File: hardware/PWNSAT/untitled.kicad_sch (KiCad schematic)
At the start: 67 parts, among them J2 Conn_01x04_Pin, J4 Conn_01x03, P4 USB_C_Plug_USB2.0, SW2 SW_Push, SW3 SW_Push, U6 W25N02KVZEIR, Y1 Crystal, Y2 24MHz

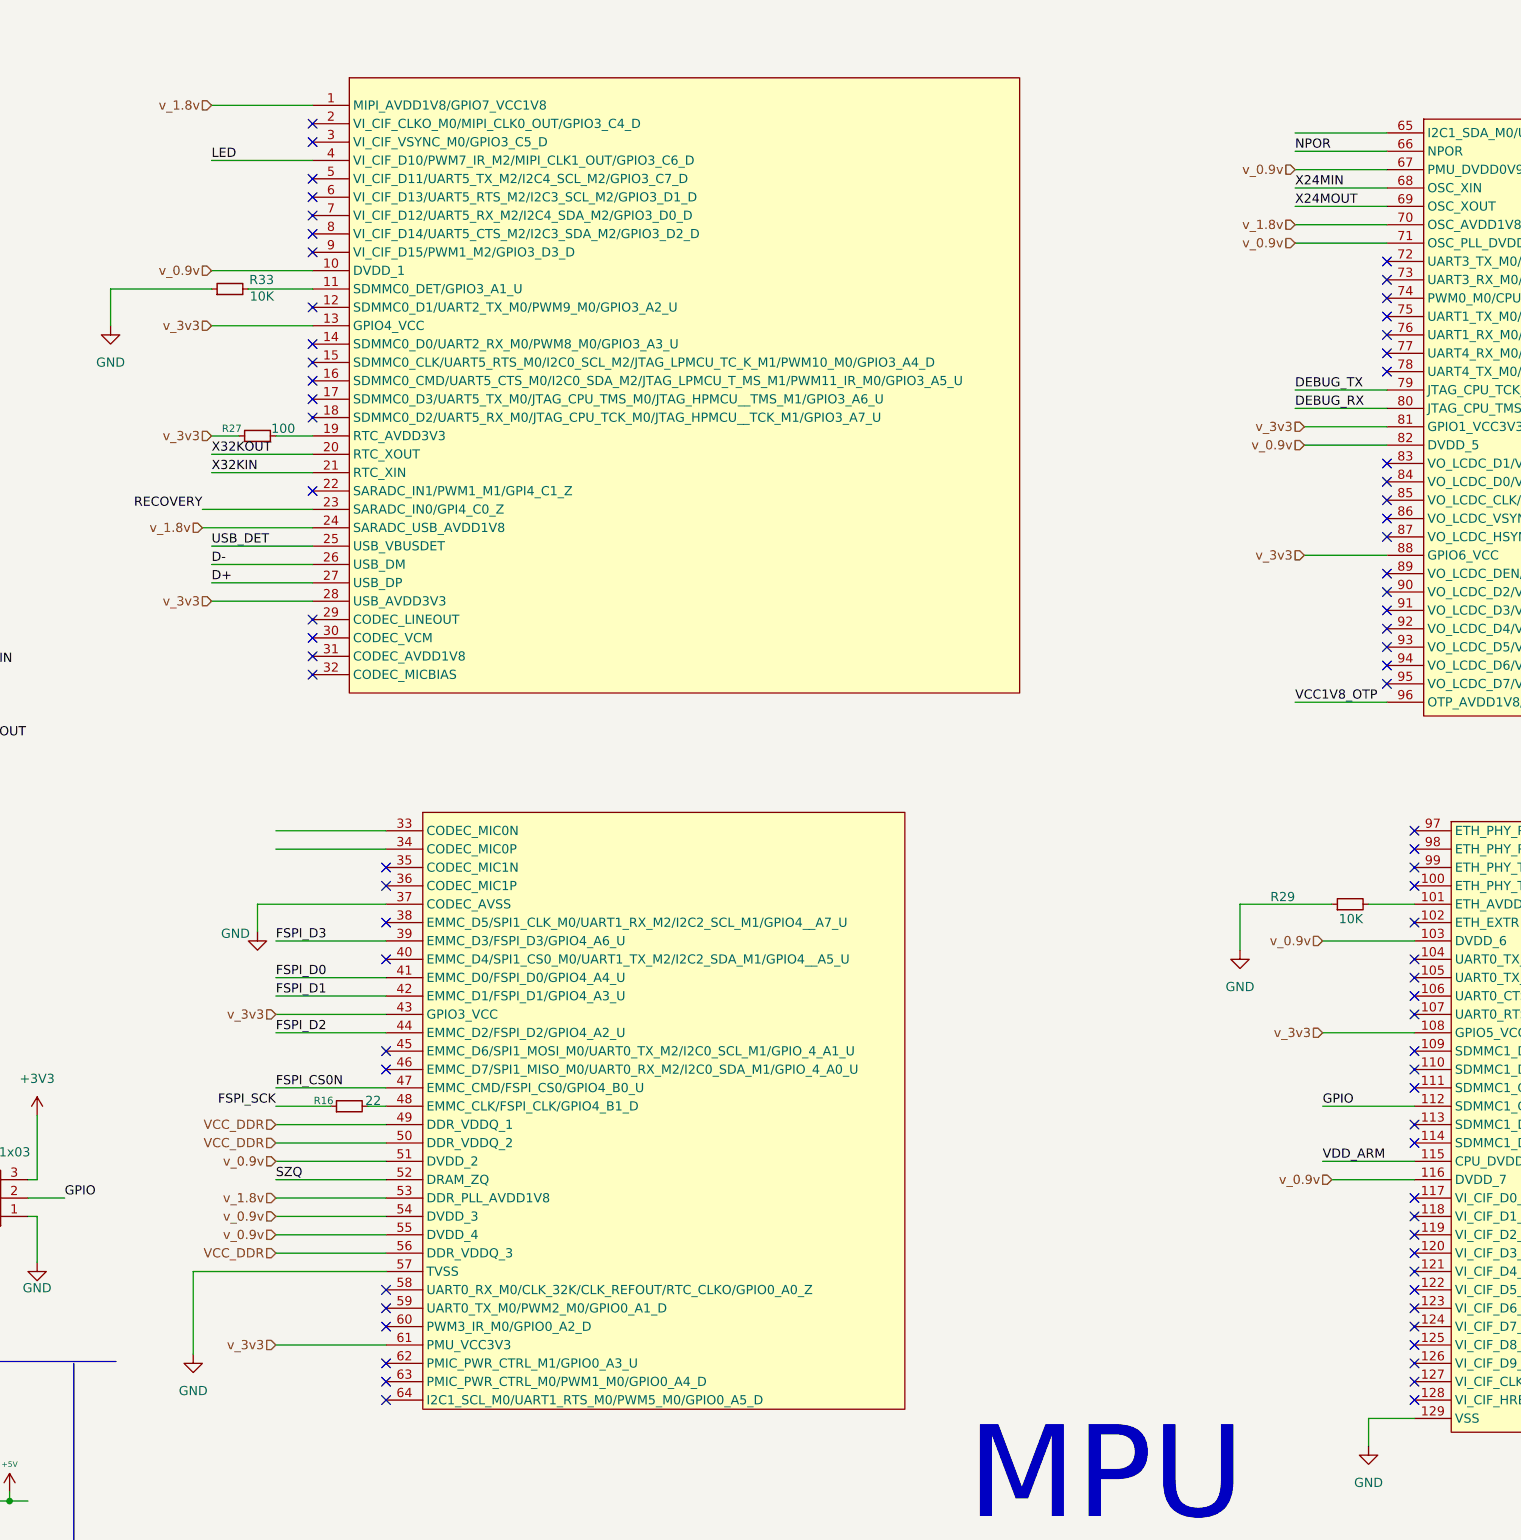
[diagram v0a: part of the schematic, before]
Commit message: Feat(hw):Added_LoRa_module
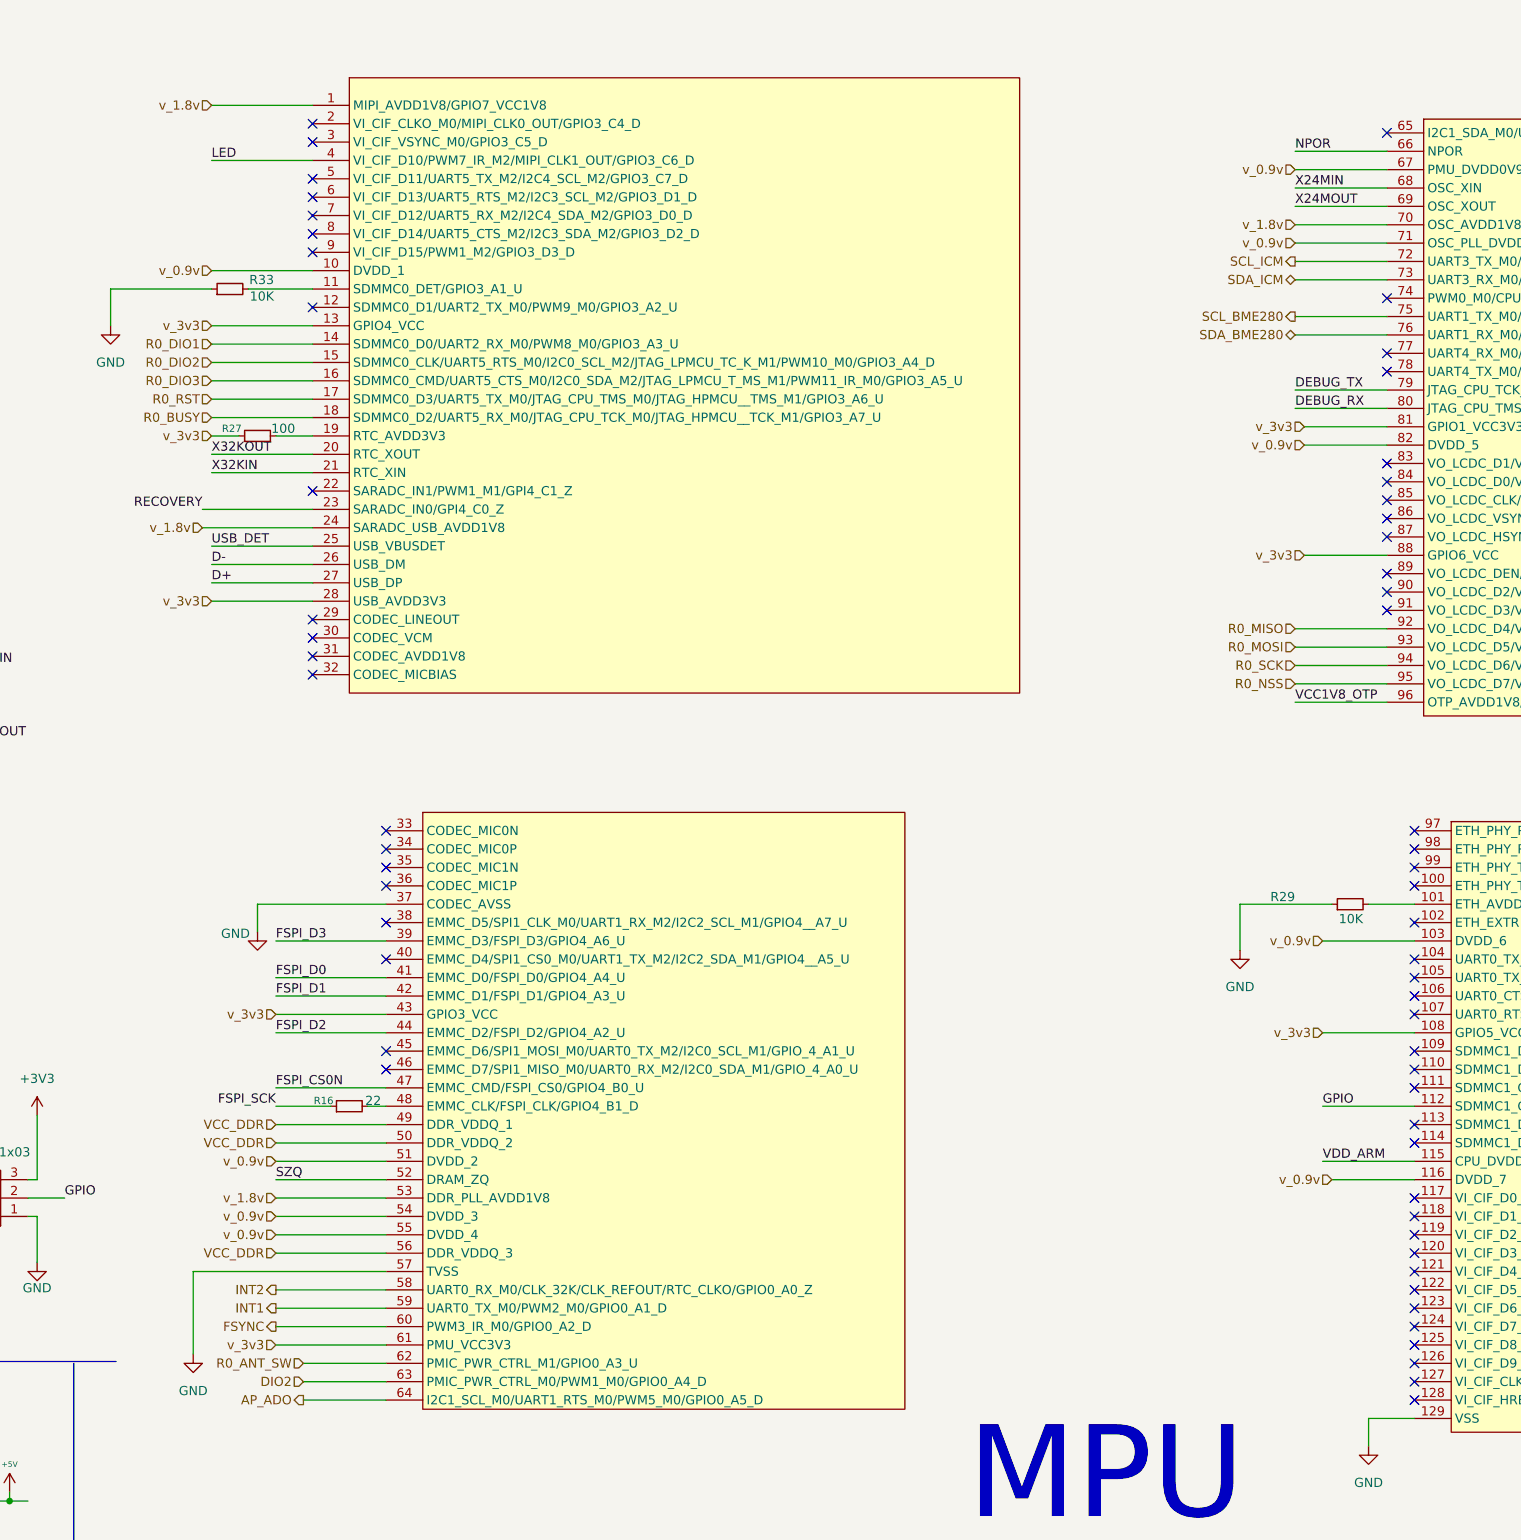
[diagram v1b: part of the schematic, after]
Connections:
- net INT2: now reaches U8.58 (UART0_RX_M0/CLK_32K/CLK_REFOUT/RTC_CLKO/GPIO0_A0_Z)
- net INT1: now reaches U8.59 (UART0_TX_M0/PWM2_M0/GPIO0_A1_D)
- net FSYNC: now reaches U8.60 (PWM3_IR_M0/GPIO0_A2_D)
- net R0_ANT_SW: now reaches U8.62 (PMIC_PWR_CTRL_M1/GPIO0_A3_U)
- net DIO2: now reaches U8.63 (PMIC_PWR_CTRL_M0/PWM1_M0/GPIO0_A4_D)
- net AP_ADO: now reaches U8.64 (I2C1_SCL_M0/UART1_RTS_M0/PWM5_M0/GPIO0_A5_D)
- net SCL_ICM: now reaches U8.72 (UART3_TX_M0/I2C2_SCL_M0/PWM7_IR_M0/GPIO1_A0__D)
- net SDA_ICM: now reaches U8.73 (UART3_RX_M0/I2C2_SDA_M0/PWM4_M0/GPIO1_A1_D)
- net SCL_BME280: now reaches U8.75 (UART1_TX_M0/I2C0_SCL_M0/GPIO1_A3_D)
- net SDA_BME280: now reaches U8.76 (UART1_RX_M0/I2C0_SDA_M0/GPIO1_A4_D)
- net R0_MISO: now reaches U8.92 (VO_LCDC_D4/VI_CIF_D5_M1/PWM6_M2/I2C4_SDA_M1/_SDMMC1_CMD_M1/SPI0_MISO_M0/GPIO1_C3_D)
- net R0_MOSI: now reaches U8.93 (VO_LCDC_D5/VI_CIF_D4_M1/PWM5_M2/I2C4_SCL_M1/_SDMMC1_CLK_M1/SPI0_MOSI_M0/GPIO1_C2_D)
- net R0_SCK: now reaches U8.94 (VO_LCDC_D6/VI_CIF_D3_M1/PWM4_M2/SPI0_CLK_M0/_SDMMC1_D0_M1/GPIO1_C1_D)
- net R0_NSS: now reaches U8.95 (VO_LCDC_D7/VI_CIF_D2_M1/PWM2_M2/SPI0_CS0_M0/_SDMMC1_D1_M1/GPIO1_C0_D)
- net R0_DIO1: now reaches U8.14 (SDMMC0_D0/UART2_RX_M0/PWM8_M0/GPIO3_A3_U)
- net R0_DIO2: now reaches U8.15 (SDMMC0_CLK/UART5_RTS_M0/I2C0_SCL_M2/JTAG_LPMCU_TC_K_M1/PWM10_M0/GPIO3_A4_D)
- net R0_DIO3: now reaches U8.16 (SDMMC0_CMD/UART5_CTS_M0/I2C0_SDA_M2/JTAG_LPMCU_T_MS_M1/PWM11_IR_M0/GPIO3_A5_U)
- net R0_RST: now reaches U8.17 (SDMMC0_D3/UART5_TX_M0/JTAG_CPU_TMS_M0/JTAG_HPMCU__TMS_M1/GPIO3_A6_U)
- net R0_BUSY: now reaches U8.18 (SDMMC0_D2/UART5_RX_M0/JTAG_CPU_TCK_M0/JTAG_HPMCU__TCK_M1/GPIO3_A7_U)
- no-connect marks 75 -> 59

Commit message: feat(Hw): Added_BOM
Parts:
- C19, C23, C26, C36, C41, C42, C49, C52, C63, C65: LCSC# (none) -> C77020
- C20, C3, C4, C6: LCSC# (none) -> C161534
- C24, C28, C34, C38, C48, C51, C60, C62, C64: LCSC# (none) -> C96446
- C25, C27, C29, C30, C35, C39, C40: LCSC# (none) -> C52923
- C5: LCSC# (none) -> C189467
- D1: LCSC# (none) -> C375573
- D2: LCSC# (none) -> C727113
- FB1, FB2: LCSC# (none) -> C14709
- H1, H2, H3, H4, J2, J4: LCSC# (none) -> ---
- R16, R17: MANUFACTURER (none) -> SG73P1JTTD22R0F
- R18: LCSC# (none) -> C131492
- R2: MANUFACTURER (none) -> CRCW0402240RFKEDHP
- R25, R27, R3: LCSC# (none) -> C253328
- R26, R29, R31, R33, R35, R36: LCSC# (none) -> C2759535
- R32: LCSC# (none) -> C323741
- R9: LCSC# (none) -> C844674
- SW2, SW3: LCSC# (none) -> C455281
- U6: LCSC# (none) -> C3010298
- U8: LCSC# (none) -> C5328706
- Y1: LCSC# (none) -> C620155
- Y2: LCSC# (none) -> C70590

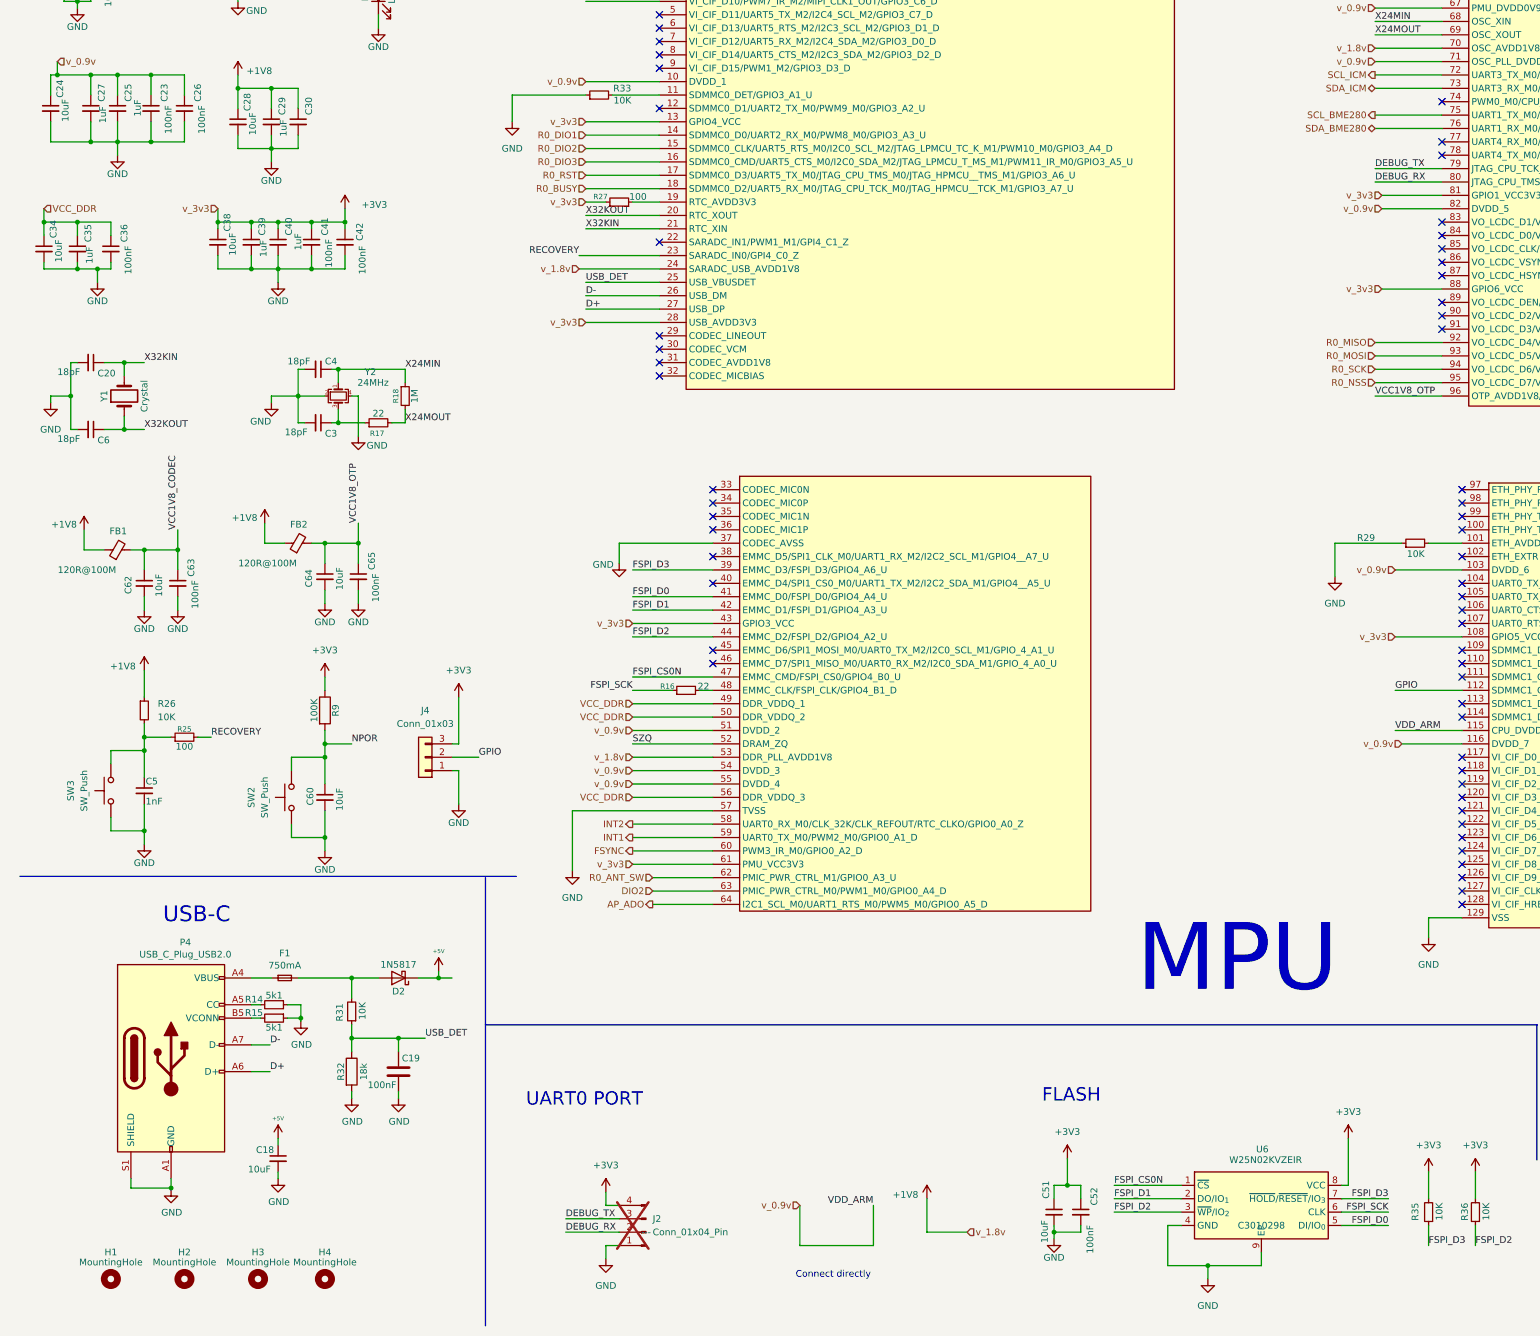
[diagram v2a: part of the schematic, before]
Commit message: feat(Hw):Sch_Updated
Pending_Sensor_Connector
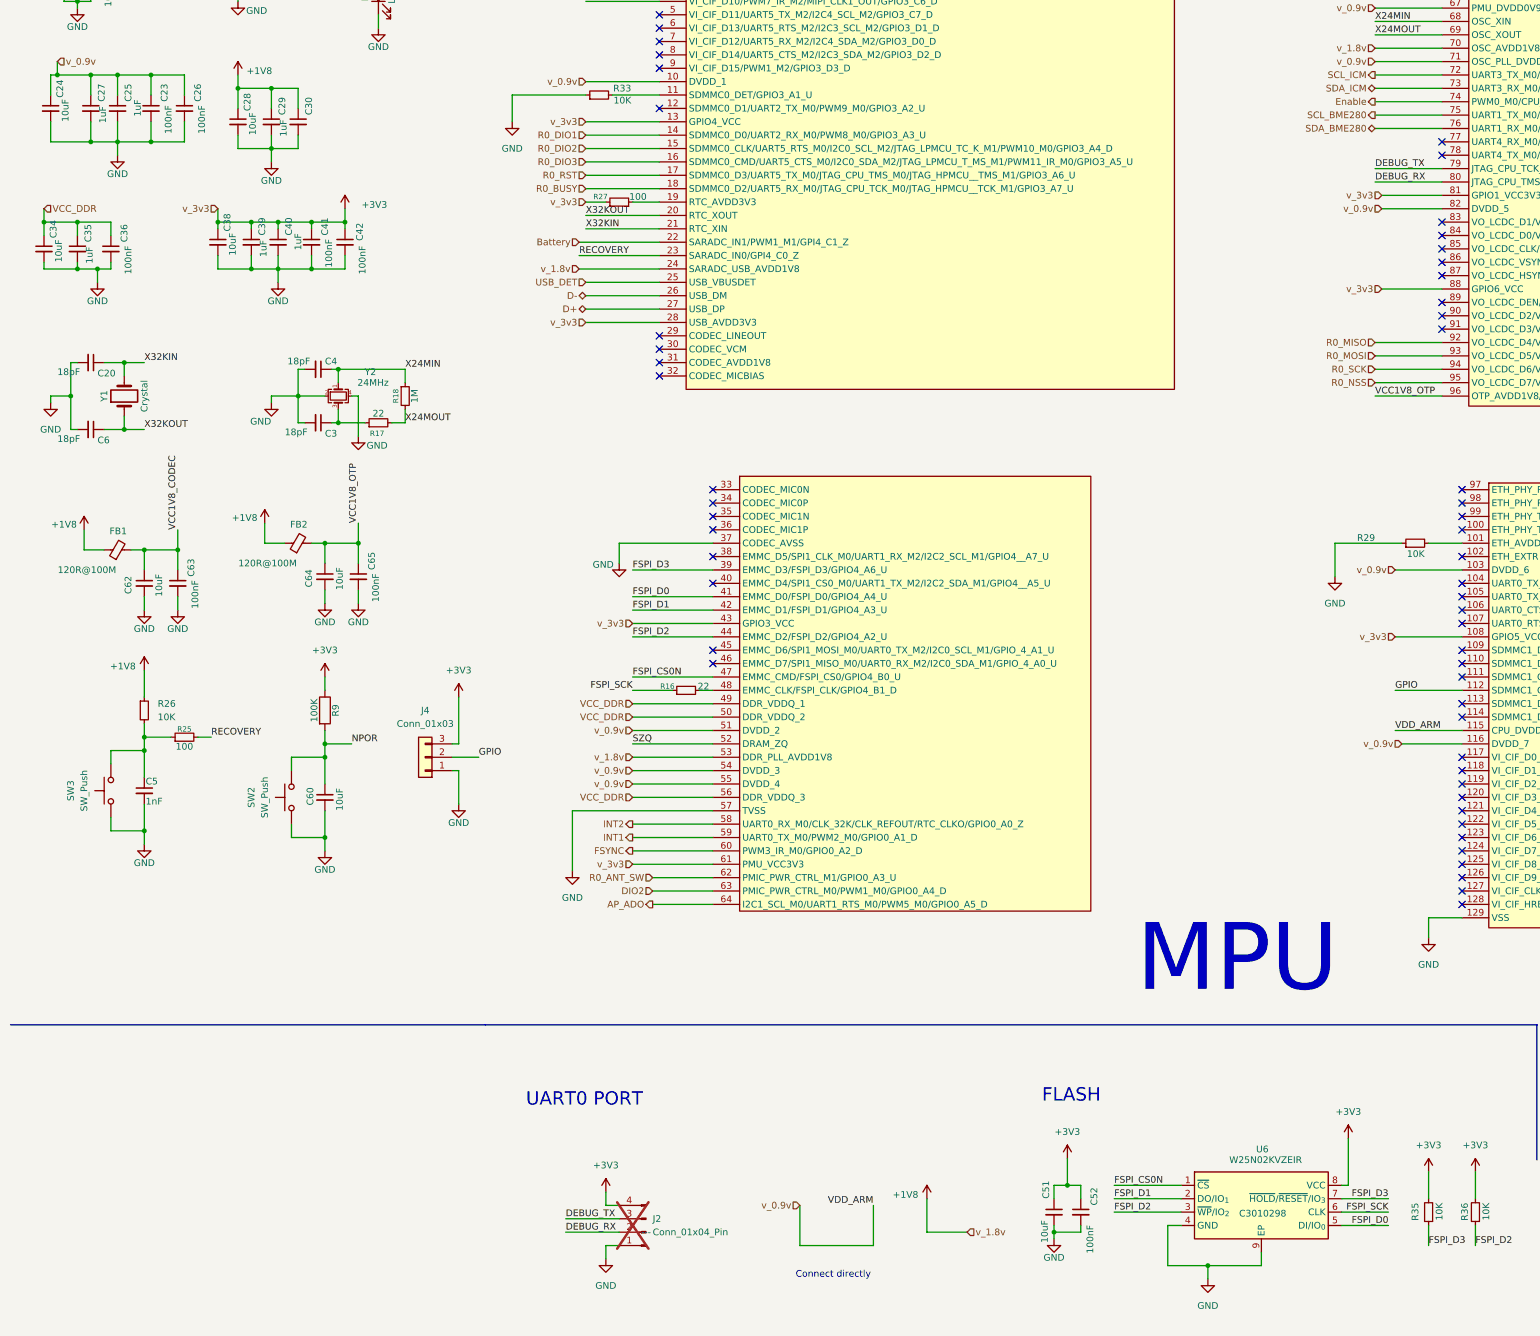
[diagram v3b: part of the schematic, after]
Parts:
- removed C18: 10uF, Capacitor_SMD:C_0402_1005Metric_Pad0.74x0.62mm_HandSolder, symbol Device:C_Small
- removed C19: 100nF, Capacitor_SMD:C_0402_1005Metric_Pad0.74x0.62mm_HandSolder, symbol Device:C
- removed D2: 1N5817, Diode_SMD:D_SOD-123F, symbol Diode:1N5817
- removed F1: 750mA, Fuse:Fuse_0603_1608Metric, symbol Device:Fuse_Small
- removed H1, H2, H3, H4: MountingHole, MountingHole:MountingHole_2.2mm_M2, symbol Mechanical:MountingHole
- removed P4: USB_C_Plug_USB2.0, pondo:C393939, symbol HunterCat-NFC-rescue:USB_C_Plug_USB2.0-Connector
- removed R14, R15: 5k1, Resistor_SMD:R_0603_1608Metric, symbol Device:R_Small
- removed R31: 10K, Resistor_SMD:R_0402_1005Metric_Pad0.72x0.64mm_HandSolder, symbol Device:R_Small
- removed R32: 18k, Resistor_SMD:R_0402_1005Metric_Pad0.72x0.64mm_HandSolder, symbol Device:R
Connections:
- net Enable: now reaches U8.74 (PWM0_M0/CPU_AVS/VI_CIF_D0_M1/GPIO1_A2_D)
- net Battery: now reaches U8.22 (SARADC_IN1/PWM1_M1/GPI4_C1_Z)
- no-connect marks 59 -> 57
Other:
- note removed: "USB-C"

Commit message: feat(Hw):Init_Floorplan
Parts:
- SW1: renamed from SW3; footprint pondo:TS1088R02026 -> PWNCube:TS1088R02026
- SW2: footprint pondo:TS1088R02026 -> PWNCube:TS1088R02026
- U1: renamed from U8; footprint pondo:RV1106G3 -> PWNCube:RV1106G3
- renumbered C48 to C1, C30 to C10, C38 to C11, C39 to C12, C40 to C13, C41 to C14, C42 to C15, C34 to C16, C35 to C17, C36 to C18, C20 to C19, C49 to C2, C4 to C20, C3 to C21, C6 to C22, C64 to C23, C65 to C24, C62 to C25, C63 to C26, C5 to C27, C60 to C28, C51 to C29, C24 to C3, C52 to C30, C27 to C4, C25 to C5, C23 to C6, C26 to C7, C28 to C8, C29 to C9, FB2 to FB1, FB1 to FB2, J4 to J1, R3 to R1, R9 to R10, R25 to R11, R35 to R12, R36 to R13, R33 to R3, R27 to R4, R18 to R5, R17 to R6, R29 to R7, R16 to R8, R26 to R9, U6 to U2

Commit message: feat(Hw):Update_Floorplan_Init_First _route
Pending_Battery_Type
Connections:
- net VCC1V8_CODEC: now also U1.31 (CODEC_AVDD1V8)
- no-connect marks 57 -> 56
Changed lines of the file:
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@@
-	)
-	(no_connect
-		(at 134.62 100.33)
 	)
 	(no_connect
@@
 		(pts
 			(xy 124.46 260.35) (xy 127 260.35)
+		)
+		(stroke
+			(width 0)
+			(type default)
+		)
+	)
+	(wire
+		(pts
+			(xy 120.65 100.33) (xy 134.62 100.33)
 		)
 		(stroke
@@
 		(effects
 			(font
+				(size 1.27 1.27)
+			)
+			(justify left bottom)
+		)
+	)
+	(label "VCC1V8_CODEC"
+		(at 120.65 100.33 0)
+		(effects
+			(font
